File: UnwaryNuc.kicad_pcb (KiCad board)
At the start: 4 copper layers, 106.1 x 63.5 mm, 171 parts, among them J1 USB_B_Micro, J2 USB_A_Dual, J3 Conn_01x06_Male, J4 RJ45_Amphenol_RJMG1BD3B8K1ANR, J5 RJ45_Amphenol_RJMG1BD3B8K1ANR, Q1 2N3904, Q2 BC856BDW1, SW1 SW_SPST, U1 NUC980DF71YC, U2 LAN8740A-EN-TR, U3 LAN8740A-EN-TR, U4 LD3985M18R_TSOT23, U5 MIC4690, U6 LM3880, U7 AP2127K-1.2, X1 ASE-xxxMHz, X2 ASE-xxxMHz, Y1 ABS07-166, Y2 NX5032GA

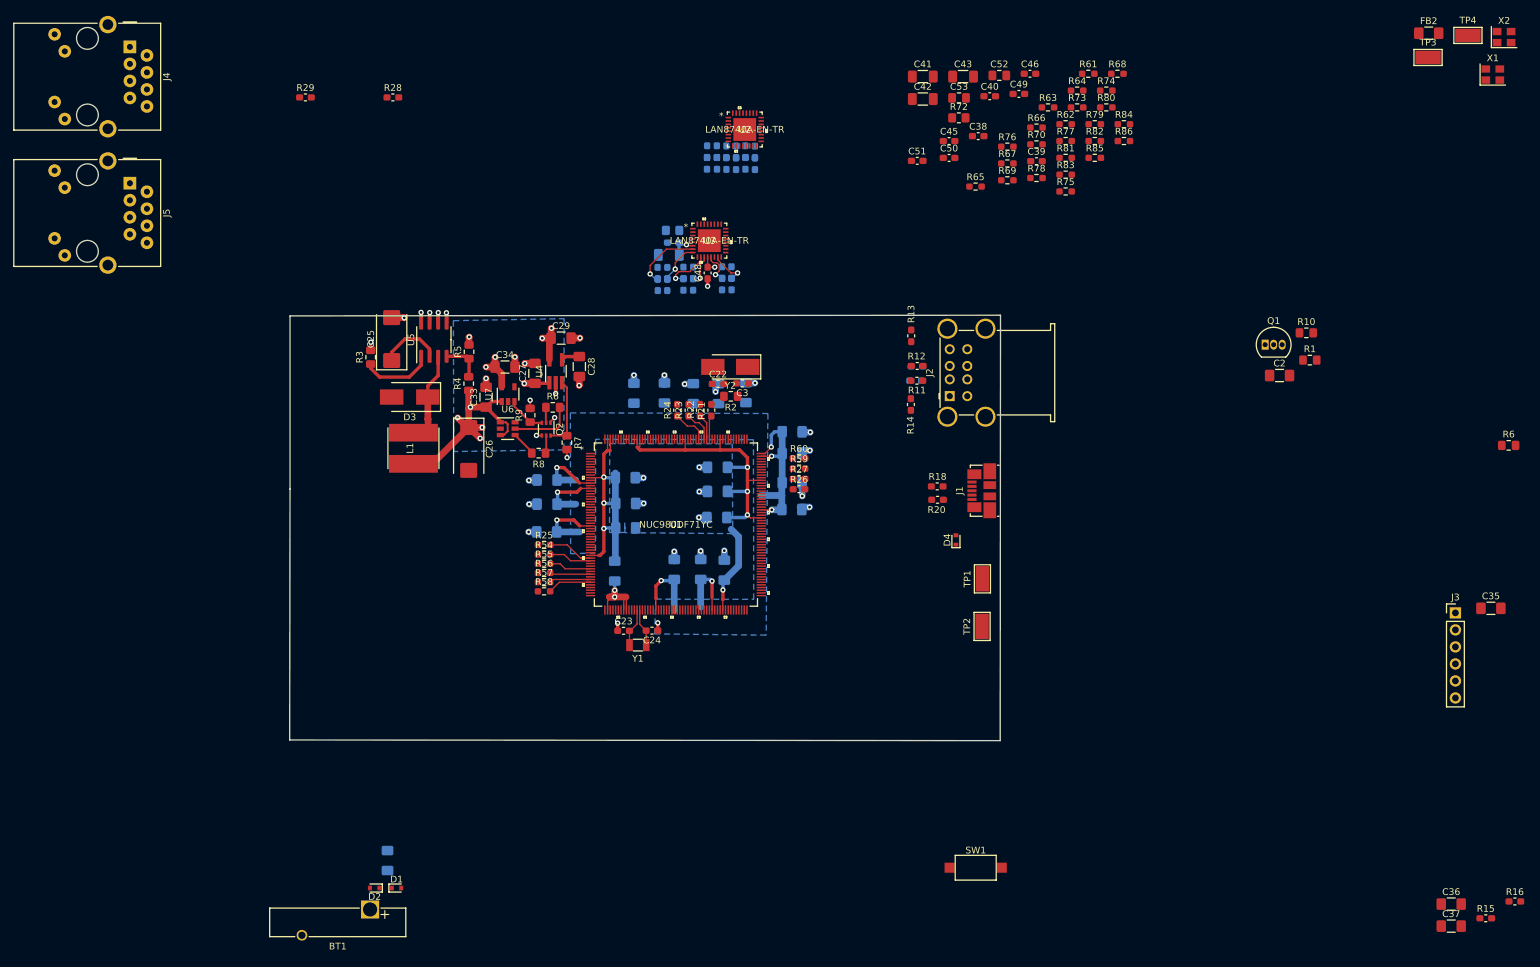
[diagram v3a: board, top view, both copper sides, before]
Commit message: added QSPI for boot, routed 1 phy, more placement completed
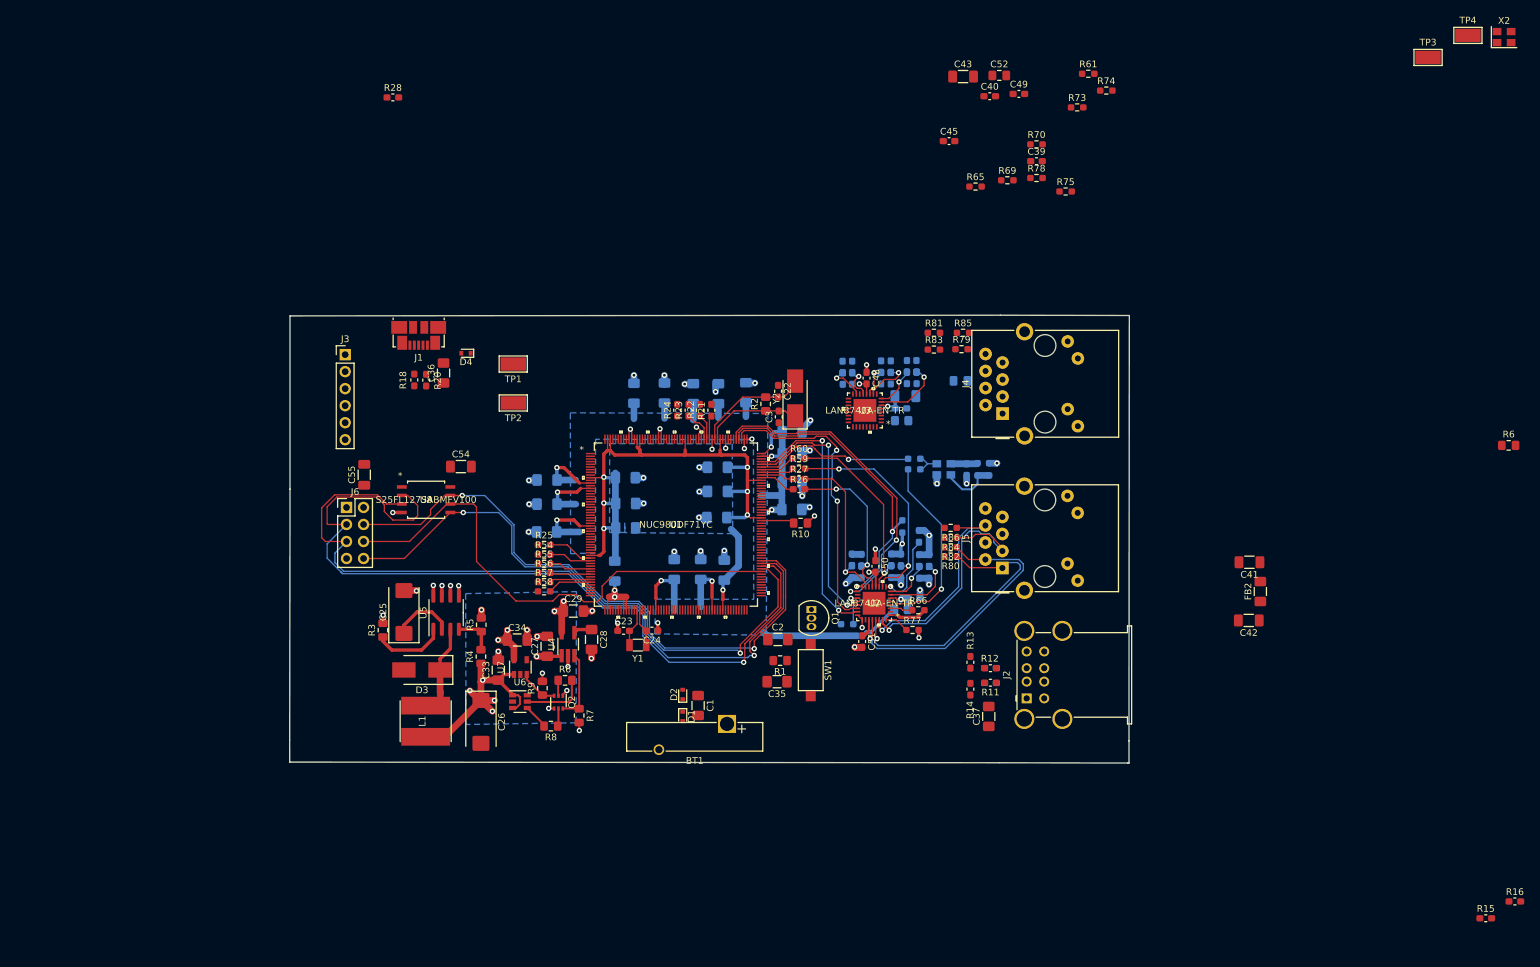
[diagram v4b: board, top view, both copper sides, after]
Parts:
- added C54: 0.1u, Capacitor_SMD:C_1206_3216Metric_Pad1.33x1.80mm_HandSolder, F.Cu at (108.2, 82.3)
- added C55: 0.1u, Capacitor_SMD:C_1206_3216Metric_Pad1.33x1.80mm_HandSolder, F.Cu at (93.8, 83.6)
- added J6: Conn_02x04_Odd_Even, Connector_PinHeader_2.54mm:PinHeader_2x04_P2.54mm_Vertical, F.Cu at (91.1, 88.4)
- added U8: S25FL127SABMFV100, UnwaryNuc:S25FL127SABMFV100, F.Cu at (103.0, 87.3)
- C1: moved to F.Cu
- C38, C46, C53, R29, R62, R63, R64, R67, R68, R72, R76, X1: moved to B.Cu
- moved J3 170.1 mm to (90.9, 65.6)
- moved C36 170.0 mm to (105.6, 68.4), turned to 90 degrees
- moved J5 142.3 mm to (189.0, 97.5), turned to 90 degrees
- moved J4 141.3 mm to (189.1, 74.4), turned to 90 degrees
- moved R29 112.6 mm to (176.6, 92.8), turned to 90 degrees
- moved C35 107.1 mm to (155.4, 114.5), turned to 180 degrees
- moved X1 100.9 mm to (180.3, 82.8), turned to 180 degrees
- moved C42 91.8 mm to (225.8, 105.3), turned to 180 degrees
- moved R1 90.9 mm to (155.9, 111.3), turned to 180 degrees
- moved C41 87.4 mm to (225.9, 96.6), turned to 180 degrees
- moved J1 87.2 mm to (101.9, 62.8), turned to 180 degrees
- moved FB2 87.0 mm to (227.5, 101.0), turned to 90 degrees
- moved C2 84.6 mm to (155.5, 108.2)
- moved R10 80.7 mm to (158.9, 90.8), turned to 180 degrees
- moved C46 80.2 mm to (175.9, 102.0), turned to 180 degrees
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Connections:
- net Net-(J4-PadR1) renamed /P0.1P
- net Net-(J4-PadR2) renamed /P0.1N
- net Net-(J4-PadR3) renamed /P0.0P
- net Net-(J4-PadR6) renamed /P0.0N
- net Net-(J5-PadR1) renamed /P1.1P
- net Net-(J5-PadR2) renamed /P1.1N
- net Net-(J5-PadR3) renamed /P1.0P
- net Net-(J5-PadR6) renamed /P1.0N
- C37 pad 2: Net-(C37-Pad2) -> VBUS
- U1 pad 111: Net-(U1-Pad111) -> /QSPI0_SS1
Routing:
- net /QSPI0_MISO0: track 0.00 -> 122.6 mm, vias 0 -> 1
- net /QSPI0_MOSI1: track 0.00 -> 114.9 mm, vias 0 -> 1
- net /QSPI0_MISO1: track 0.00 -> 92.3 mm, vias 0 -> 2
- net /QSPI0_MOSI0: track 0.00 -> 88.5 mm, vias 0 -> 2
- net /QSPI0_CLK: track 0.00 -> 76.1 mm
- net /RMII1_MDC: track 0.00 -> 48.7 mm, vias 0 -> 2
- net /RMII1_MDIO: track 0.00 -> 47.7 mm, vias 0 -> 2
- net /RMII1_TXD0: track 0.00 -> 44.2 mm, vias 0 -> 2
- net /P1.1N: track 0.00 -> 43.5 mm, vias 0 -> 1
- net /P1.1P: track 0.00 -> 41.5 mm, vias 0 -> 1
- net +1V2: track 85.9 -> 127.2 mm, vias 10 -> 13
- net /RMII1_TXD1: track 0.00 -> 39.8 mm, vias 0 -> 2
- net /P1.0P: track 0.00 -> 39.5 mm, vias 0 -> 1
- net /RMII1_TXEN: track 0.00 -> 38.1 mm, vias 0 -> 2
- net /PHY.RMII1_RXD1\P1MODE1: track 0.00 -> 34.1 mm, vias 0 -> 2
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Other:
- board size 106.1 x 63.5 mm -> 125.3 x 66.8 mm

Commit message: started other phy
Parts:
- removed the R6 at (264.6, 79.2)
- C45, C52, R69, R70, R73, R74, R78, X2: moved to B.Cu
- moved R15 152.0 mm to (128.7, 75.2)
- moved R16 150.8 mm to (133.1, 75.1)
- moved X2 117.4 mm to (155.7, 63.8), turned to 180 degrees
- moved R28 84.6 mm to (171.7, 68.9), turned to 90 degrees
- moved C40 78.8 mm to (177.4, 105.2), turned to 180 degrees
- moved C52 71.9 mm to (182.5, 95.6), turned to 270 degrees
- moved R74 64.7 mm to (152.0, 64.0)
- moved R73 55.3 mm to (155.5, 61.3), turned to 180 degrees
- moved R78 47.8 mm to (163.7, 76.2), turned to 180 degrees
- moved R70 44.7 mm to (160.6, 63.8), turned to 90 degrees
- moved C39 43.5 mm to (175.0, 75.8), turned to 180 degrees
- moved R75 43.0 mm to (175.0, 77.3)
- moved C45 37.2 mm to (158.9, 63.7), turned to 270 degrees
- moved R69 36.5 mm to (162.4, 63.8), turned to 90 degrees
- moved R65 35.3 mm to (175.1, 74.4)
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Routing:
- net /RMII0_TXD0: track 0.00 -> 48.4 mm, vias 0 -> 2
- net /RMII0_MDIO: track 0.00 -> 47.1 mm, vias 0 -> 2
- net /RMII0_TXD1: track 0.00 -> 46.8 mm, vias 0 -> 2
- net /RMII0_TXEN: track 0.61 -> 44.7 mm, vias 0 -> 2
- net /PHY.RMII0_RXD1\P0MODE1: track 6.88 -> 50.8 mm, vias 1 -> 2
- net /RMII0_MDC: track 0.00 -> 43.6 mm, vias 0 -> 2
- net /P0.1N: track 0.00 -> 39.9 mm, vias 0 -> 1
- net /P0_XTALI: track 0.00 -> 38.6 mm, vias 0 -> 1
- net /P0.0P: track 0.00 -> 38.0 mm, vias 0 -> 1
- net /P0.1P: track 0.00 -> 37.5 mm, vias 0 -> 1
- net /PHY.RMII0_RXD0\P0MODE0: track 4.49 -> 40.3 mm
- net /RMII0_REFCLK: track 0.00 -> 33.6 mm, vias 0 -> 1
- net /P0.0N: track 0.00 -> 31.1 mm, vias 0 -> 1
- net VDDA: track 14.8 -> 42.9 mm, vias 0 -> 4
- net /PHY.RMII0_RXERR\P0AD0: track 4.92 -> 32.4 mm, vias 1 -> 2
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
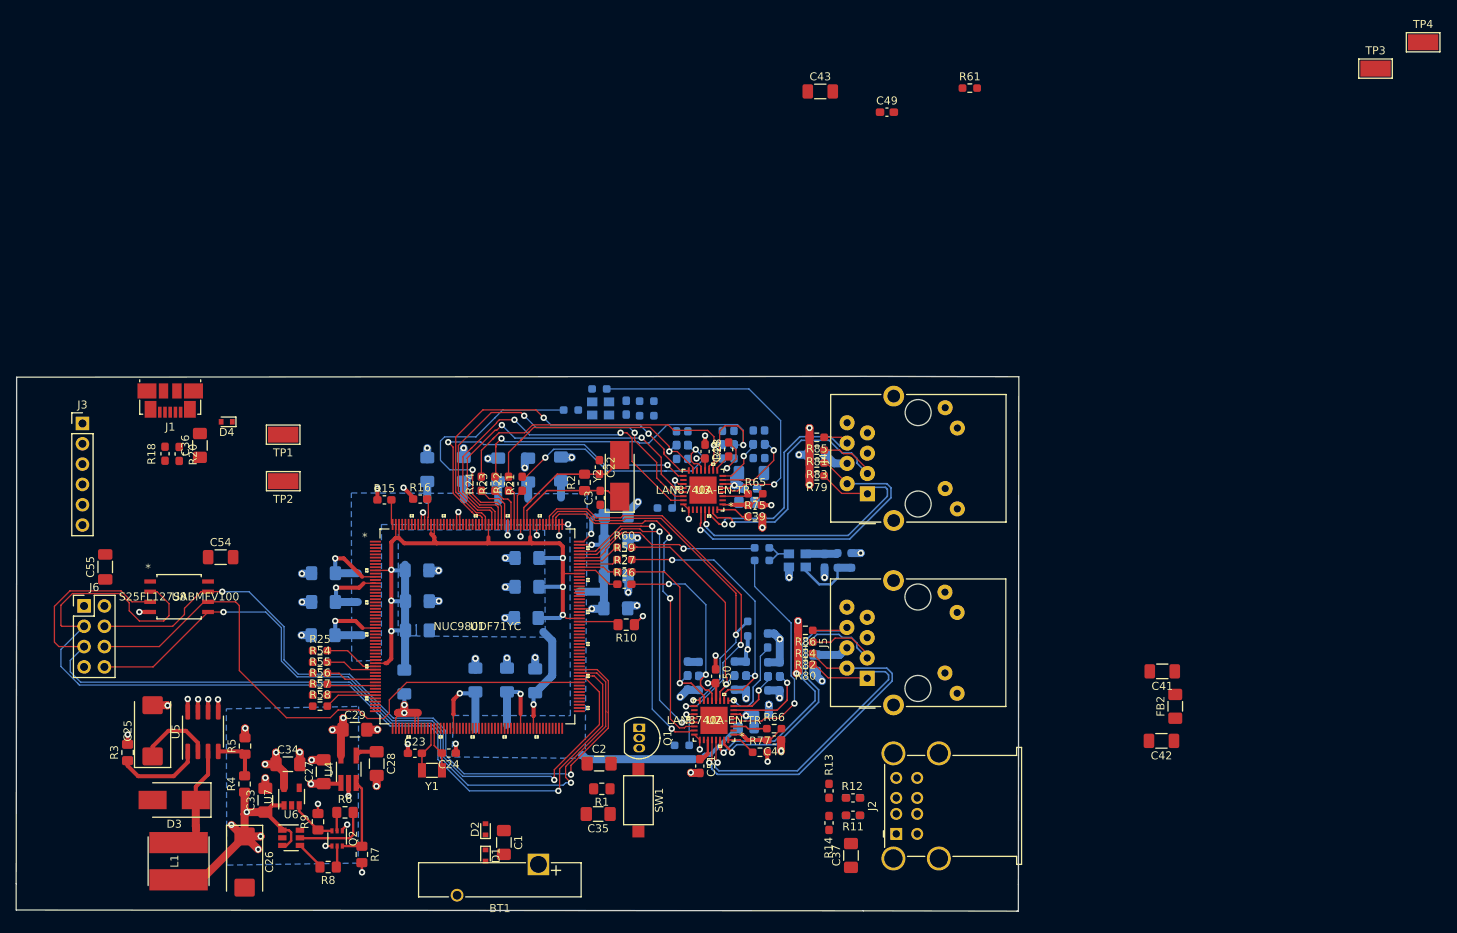
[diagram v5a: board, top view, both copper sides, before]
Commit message: Signal routing pretty much done, working out power distribution. Still could/should add Headers for other I/O, and an ESP backpack or something
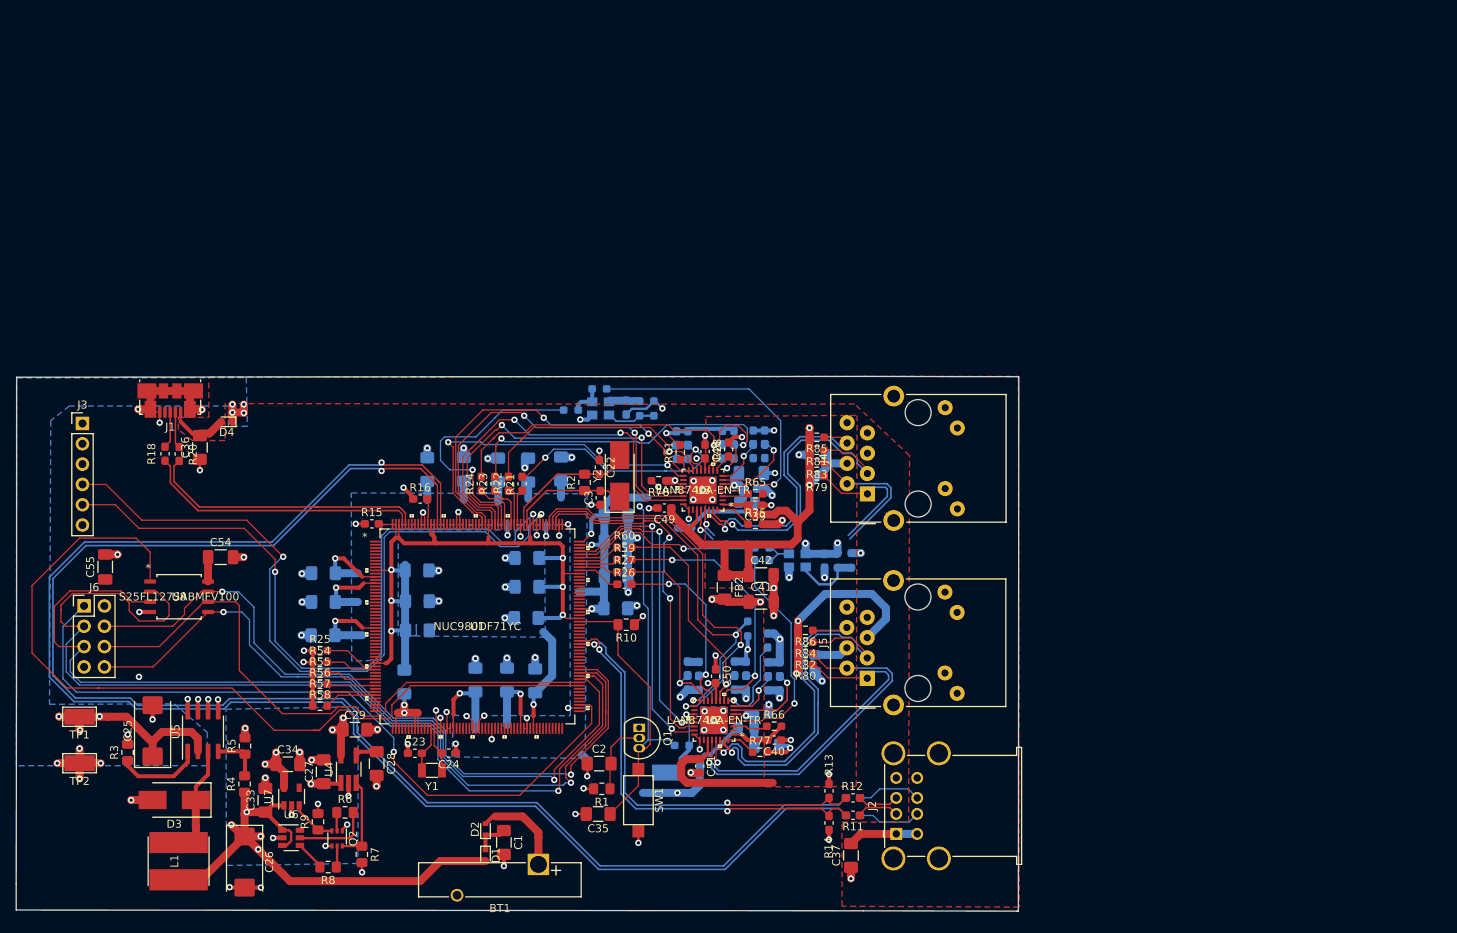
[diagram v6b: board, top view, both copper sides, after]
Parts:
- removed TP3: TestPoint, TestPoint:TestPoint_Keystone_5019_Minature
- C43, TP4: moved to B.Cu
- R78: moved to F.Cu
- moved TP4 131.4 mm to (164.0, 109.3)
- moved C43 82.1 mm to (176.5, 105.9)
- moved FB2 58.3 mm to (171.2, 86.1), turned to 270 degrees
- moved R61 58.2 mm to (165.7, 69.2), turned to 90 degrees
- moved C49 56.8 mm to (163.7, 76.2), turned to 180 degrees
- moved C42 54.2 mm to (175.8, 84.6), turned to 0 degrees
- moved C41 50.9 mm to (175.8, 87.9), turned to 0 degrees
- moved TP1 43.5 mm to (90.6, 102.3)
- moved TP2 43.5 mm to (90.6, 108.1)
- moved R78 3.49 mm to (163.0, 72.8)
- moved R15 3.39 mm to (127.1, 78.2)
- moved R75 0.92 mm to (175.1, 78.2)
- moved R66 0.30 mm to (177.4, 103.5)
- moved C36 0.25 mm to (105.6, 68.6)
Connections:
- net Net-(R17-Pad1) renamed /USB1_P
- net Net-(R19-Pad2) renamed /USB1_N
- R76 pad 1: Net-(R76-Pad1) -> /P1_nRST
- U2 pad 19: Net-(R76-Pad1) -> /P1_nRST
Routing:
- net /USB1_N: track 0.00 -> 188.8 mm, vias 0 -> 1
- net /USB1_P: track 0.00 -> 186.7 mm, vias 0 -> 1
- net GND: track 92.1 -> 200.1 mm, vias 62 -> 112
- net /QSPI0_SS0: track 0.00 -> 107.5 mm, vias 0 -> 1
- net /UART0_RXD: track 0.00 -> 96.0 mm, vias 0 -> 2
- net /QSPI0_SS1: track 0.00 -> 91.5 mm, vias 0 -> 1
- net /UART0_TXD: track 0.00 -> 90.8 mm, vias 0 -> 2
- net VDDA: track 42.9 -> 131.4 mm
- net /nRST: track 4.99 -> 73.0 mm, vias 0 -> 2
- net +3V3: track 175.7 -> 238.7 mm, vias 20 -> 27
- net /USBHL.DD_N: track 0.00 -> 53.5 mm, vias 0 -> 2
- net /USBHL.DD_P: track 0.00 -> 53.4 mm, vias 0 -> 2
- net /USB0.DD_N: track 0.00 -> 35.1 mm
- net /USB0.DD_P: track 0.00 -> 35.0 mm
- net +1V2: track 128.1 -> 162.7 mm, vias 13 -> 16
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- added copper zone on L3_(Sig), net +3V3
- added copper zone on B.Cu, net +5V
- added copper zone on B.Cu, net GND
- added copper zone on L2_(Plane), net GND
- added copper zone on F.Cu, net VBUS
- added copper zone on F.Cu, net VDDA
